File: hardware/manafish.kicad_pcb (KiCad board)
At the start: 2 copper layers, 70 x 100 mm, 57 parts, among them IC1 BMI270, IC2 SHT45-AD1F-R2, J1 Conn_01x04_Pin, J2 SM03B-SRSS-TB, J3 AM32_1, J4 AM32_2, J5 Conn_01x22_Female, J6 Battery, J7 Conn_02x07_Odd_Even, J8 USB_C_Receptacle_USB2.0_14P, U1 TPD4EUSB30, U2 TPD4EUSB30, U3 MagJack-A70-112-331N126, U4 RP2354A, U5 Ag5724-LPB, Y1 ABM8-272-T3

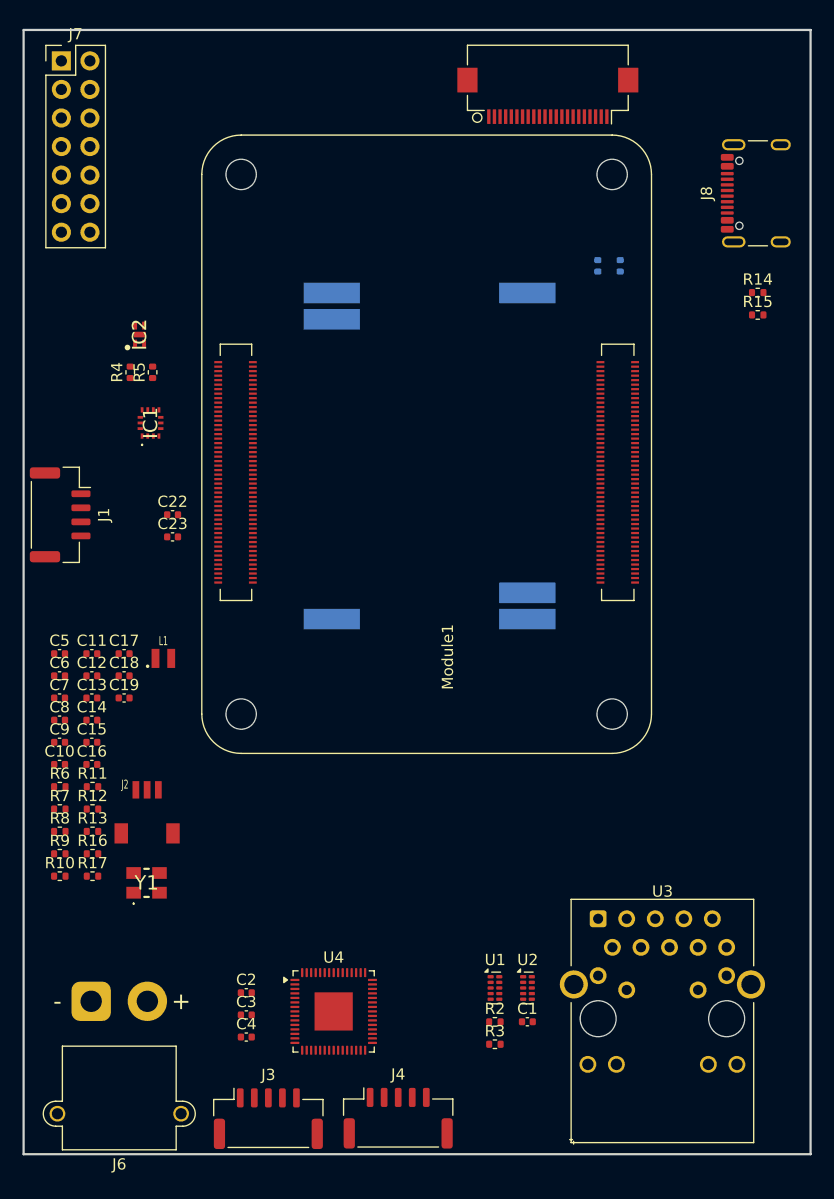
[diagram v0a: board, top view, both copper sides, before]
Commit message: Add PoE circuit
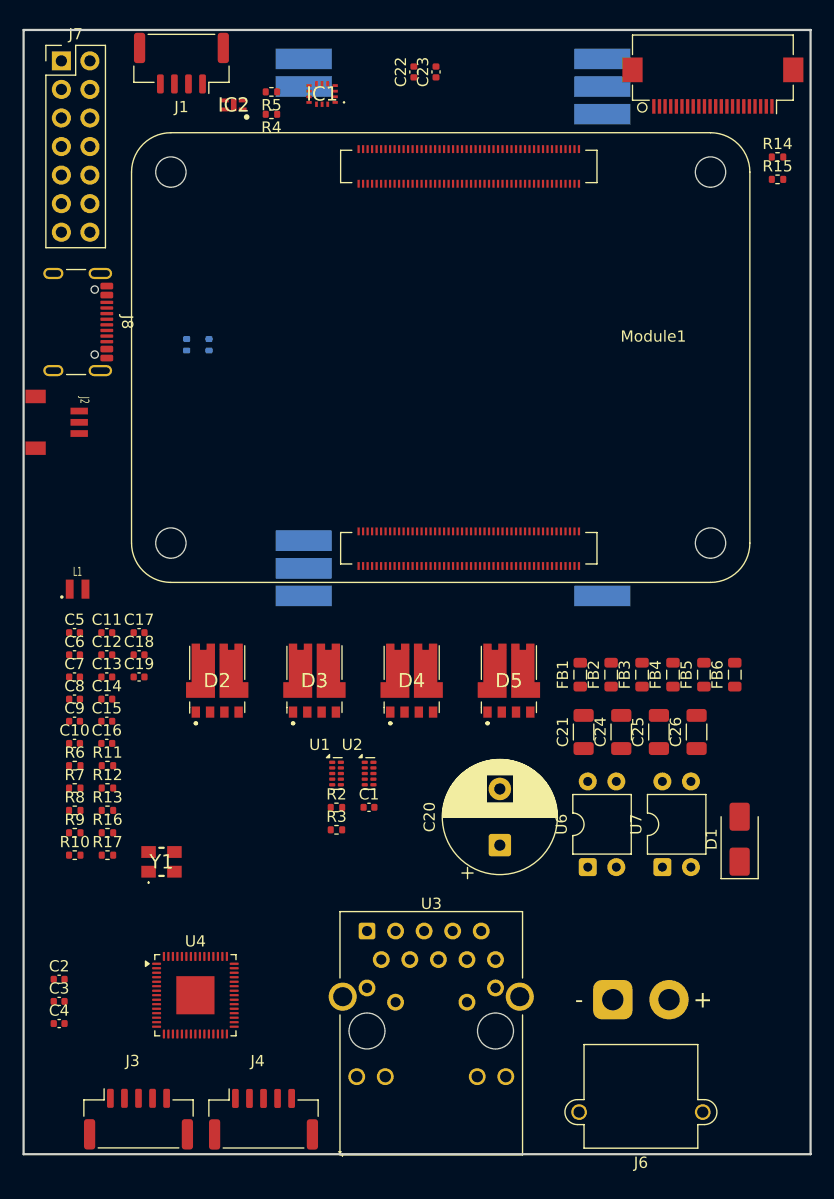
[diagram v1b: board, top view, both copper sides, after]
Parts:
- added C20: 470uF 25V, Capacitor_THT:CP_Radial_D10.0mm_P5.00mm, F.Cu at (129.5, 121.0)
- added C21: 4.7nF 2kV, Capacitor_SMD:C_1206_3216Metric, F.Cu at (137.0, 110.9)
- added C24: 4.7nF 2kV, Capacitor_SMD:C_1206_3216Metric, F.Cu at (140.3, 110.9)
- added C25: 100nF 25V, Capacitor_SMD:C_1206_3216Metric, F.Cu at (143.7, 110.9)
- added C26: 10uF 25V, Capacitor_SMD:C_1206_3216Metric, F.Cu at (147.0, 110.9)
- added D1: SMAJ58A, Diode_SMD:D_SMA, F.Cu at (150.8, 120.4)
- added D2: V6K100DUHM3_H, V6K100DUHM3:V6K100DUHM3H, F.Cu at (104.4, 106.2)
- added D3: V6K100DUHM3_H, V6K100DUHM3:V6K100DUHM3H, F.Cu at (113.0, 106.2)
- added D4: V6K100DUHM3_H, V6K100DUHM3:V6K100DUHM3H, F.Cu at (121.7, 106.2)
- added D5: V6K100DUHM3_H, V6K100DUHM3:V6K100DUHM3H, F.Cu at (130.3, 106.2)
- added FB1: 1kR 1.5A, Inductor_SMD:L_0805_2012Metric, F.Cu at (136.7, 105.8)
- added FB2: 1kR 1.5A, Inductor_SMD:L_0805_2012Metric, F.Cu at (139.4, 105.8)
- added FB3: 1kR 1.5A, Inductor_SMD:L_0805_2012Metric, F.Cu at (142.2, 105.8)
- added FB4: 1kR 1.5A, Inductor_SMD:L_0805_2012Metric, F.Cu at (144.9, 105.8)
- added FB5: 1kR 1.5A, Inductor_SMD:L_0805_2012Metric, F.Cu at (147.7, 105.8)
- added FB6: 1kR 1.5A, Inductor_SMD:L_0805_2012Metric, F.Cu at (150.4, 105.8)
- added U6: PC817, Package_DIP:DIP-4_W7.62mm, F.Cu at (137.3, 122.9)
- added U7: PC817, Package_DIP:DIP-4_W7.62mm, F.Cu at (144.0, 122.9)
- U5: value Ag5724-LPB -> Ag59824-LPB; footprint Silvertel:Silvertel_Ag5700-LPB -> Silvertel:Silvertel_Ag59800-LPB
- moved J8 63.6 mm to (90.9, 74.4), turned to -90 degrees
- moved C23 47.5 mm to (123.8, 52.2), turned to 90 degrees
- moved J6 46.4 mm to (139.6, 134.7)
- moved C22 44.9 mm to (121.9, 52.2), turned to 90 degrees
- moved Module1 44.4 mm to (148.2, 94.1), turned to 90 degrees
- moved J1 41.6 mm to (101.2, 51.4), turned to 180 degrees
- moved J2 38.7 mm to (87.5, 83.3), turned to -90 degrees
- moved R19 37.2 mm to (103.6, 76.5)
- moved R18 37.2 mm to (101.7, 76.5)
- moved IC1 33.0 mm to (113.7, 54.1), turned to 180 degrees
- moved R5 27.1 mm to (109.2, 54.0), turned to 180 degrees
- moved R4 26.2 mm to (109.2, 56.0), turned to 180 degrees
- moved R2 23.7 mm to (115.0, 117.6)
- moved C1 23.7 mm to (117.9, 117.6)
- moved U2 23.7 mm to (117.9, 114.6)
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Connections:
- Module1 pad 30: unconnected-(Module1A-GPIO6-Pad30) -> /Power Management/POE_TYP2_DET
- Module1 pad 31: unconnected-(Module1A-GPIO12-Pad31) -> /Power Management/POE_TYP3_DET
- U3 pad 11: /Ethernet/TR0_TAP -> /Ethernet/VC1
- U3 pad 12: /Ethernet/TR1_TAP -> /Ethernet/VC2
- U3 pad 13: /Ethernet/TR2_TAP -> /Ethernet/VC3
- U3 pad 14: /Ethernet/TR3_TAP -> /Ethernet/VC4
- U5 pad 1: unconnected-(U5-+VDC-Pad1) -> Net-(U5-VIN-)
- U5 pad 2: unconnected-(U5--VDC-Pad2) -> Net-(U5-TYP3-DET)
- U5 pad 3: unconnected-(U5-ADJ-Pad3) -> Net-(U5-TYP2-DET)
- U5 pad 4: unconnected-(U5-VIN+-Pad4) -> /Power Management/24V
- U5 pad 5: unconnected-(U5-TYP2-DET-Pad5) -> /Power Management/24V
- U5 pad 6: unconnected-(U5-VIN--Pad6) -> GND

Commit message: Finished power management circuit
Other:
- board text added: "Note: Rohrdurchmesser: 74,5mm Max. PCB Länge: 110mm"
- board text removed: "Note: Rohrdurchmesser: 74,5mm Max. PCB Länge: 105mm"
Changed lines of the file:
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@@
 		(layer "Edge.Cuts")
 	)
-	(gr_text "Note: Rohrdurchmesser: 74,5mm\n      Max. PCB Länge: 105mm"
+	(gr_text "Note: Rohrdurchmesser: 74,5mm\n      Max. PCB Länge: 110mm"
 		(at 14.675 19.425 0)
 		(layer "Cmts.User")
